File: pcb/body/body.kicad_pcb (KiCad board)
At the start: 2 copper layers, 55 x 90 mm, 146 parts, among them J1 Conn_01x05_Pin, J2 Conn_01x08_Socket, J3 Output_1_2, J4 Output_3_4, J5 Headphones, J6 Headphones, J7 Headphones, J8 Barrel_Jack_Switch, J9 Battery_Power, U1 Teensy4.1, U10 SGTL5000XNLA3, U2 TL072, U3 TL072, U4 TL072, U5 AP7313-18SAG, U6 SGTL5000XNLA3, U7 TPS54331DR, U8 SGTL5000XNLA3

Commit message: initial layout
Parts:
- removed the J6 at (124.3, 121.9)
- removed the J7 at (99.5, 121.9)
- removed the R11 at (13.6, 44.2)
- removed the R23 at (148.4, 105.0)
- removed the R25 at (148.4, 109.1)
- removed the R37 at (14.6, 12.1)
- removed the R39 at (14.6, 16.2)
- removed the R9 at (13.6, 40.1)
- added RV1: 10k, Potentiometer_THT:Potentiometer_Bourns_3296W_Vertical, F.Cu at (62.5, 110.0)
- added RV2: 10k, Potentiometer_THT:Potentiometer_Bourns_3296W_Vertical, F.Cu at (74.5, 110.0)
- added RV3: 10k, Potentiometer_THT:Potentiometer_Bourns_3296W_Vertical, F.Cu at (35.0, 126.0)
- added RV4: 10k, Potentiometer_THT:Potentiometer_Bourns_3296W_Vertical, F.Cu at (46.0, 126.0)
- added RV5: 10k, Potentiometer_THT:Potentiometer_Bourns_3296W_Vertical, F.Cu at (9.08, 126.0)
- added RV6: 10k, Potentiometer_THT:Potentiometer_Bourns_3296W_Vertical, F.Cu at (20.1, 126.0)
- J1, U1: moved to B.Cu
- J5: value Headphones -> AudioJack3_SwitchTR; footprint Connector_PinHeader_2.54mm:PinHeader_1x03_P2.54mm_Vertical -> Connector_Audio:Jack_3.5mm_CUI_SJ1-3525N_Horizontal
- moved C9 109.1 mm to (75.0, 115.0), turned to 90 degrees
- moved R16 108.0 mm to (36.8, 97.0)
- moved R17 108.0 mm to (36.8, 99.5)
- moved R18 108.0 mm to (36.8, 102.0)
- moved R19 108.0 mm to (36.8, 109.5)
- moved R20 108.0 mm to (36.8, 112.0)
- moved C12 108.0 mm to (28.8, 97.0)
- moved C13 108.0 mm to (28.8, 99.5)
- moved C14 108.0 mm to (28.8, 102.0)
- moved C15 108.0 mm to (28.8, 104.5)
- moved C16 108.0 mm to (28.8, 107.0)
- moved C17 108.0 mm to (28.8, 109.5)
- moved C18 108.0 mm to (28.8, 112.0)
- moved C19 108.0 mm to (28.8, 114.5)
- moved D3 108.0 mm to (41.2, 98.0)
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- renumbered C46 to C19, C47 to C20, C48 to C21, C49 to C22, C50 to C23, C51 to C24, C52 to C25, C53 to C26, C54 to C27, C55 to C28, C56 to C29, C57 to C30, C58 to C31, C59 to C32, C60 to C33, C19 to C34, C20 to C35, C21 to C36, C22 to C37, C23 to C38, C24 to C39, C25 to C40, C26 to C41, C27 to C42, C28 to C43, C29 to C44, C30 to C45, C31 to C46, C32 to C47, C33 to C48, C34 to C49, C35 to C50, C36 to C51, C37 to C52, C38 to C53, C39 to C54, C40 to C55, C41 to C56, C42 to C57, C43 to C58, C44 to C59, C45 to C60, C68 to C65, C65 to C66, C66 to C68, J8 to J6, J9 to J7, JP7 to JP1, R14 to R10, R15 to R11, R16 to R12, R17 to R13, R18 to R14, R19 to R15, R20 to R16, R21 to R17, R22 to R18, R27 to R19, R28 to R20, R29 to R21, R30 to R22, R31 to R23, R32 to R24, R33 to R25, R34 to R26, R35 to R27, R36 to R28, R41 to R29, R42 to R30, R49 to R31, R50 to R32, R51 to R33, R52 to R34, R53 to R35, R54 to R36, R55 to R37, R56 to R38, R57 to R39, R43 to R40, R44 to R41, R45 to R42, R13 to R9, U6 to U5, U8 to U6, U10 to U7, U7 to U8, U5 to U9
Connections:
- U5 pad 1: Net-(J5-Pin_1) -> /codec1/HEADPHONES_L
- U5 pad 2: Net-(J5-Pin_2) -> /codec1/HEADPHONES_GND
- U5 pad 4: Net-(J5-Pin_3) -> /codec1/HEADPHONES_R
- U6 pad 1: Net-(J6-Pin_1) -> /codec2/HEADPHONES_L
- U6 pad 2: Net-(J6-Pin_2) -> /codec2/HEADPHONES_GND
- U6 pad 4: Net-(J6-Pin_3) -> /codec2/HEADPHONES_R
- U7 pad 1: Net-(J7-Pin_1) -> /codec3/HEADPHONES_L
- U7 pad 2: Net-(J7-Pin_2) -> /codec3/HEADPHONES_GND
- U7 pad 4: Net-(J7-Pin_3) -> /codec3/HEADPHONES_R
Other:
- board size 55 x 90 mm -> 80 x 120 mm

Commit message: lots more layout
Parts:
- removed the C36 at (136.8, 125.8)
- removed the C41 at (140.8, 125.8)
- removed the C42 at (140.8, 128.3)
- removed the C45 at (112.0, 125.8)
- removed the C50 at (116.0, 125.8)
- removed the C51 at (116.0, 128.3)
- removed the C54 at (87.2, 125.8)
- removed the C59 at (91.2, 125.8)
- removed the C60 at (91.2, 128.3)
- removed the J3 at (90.0, 38.2)
- removed the R31 at (144.8, 120.8)
- removed the R32 at (144.8, 123.3)
- removed the R34 at (120.0, 120.8)
- removed the R35 at (120.0, 123.3)
- removed the R37 at (95.2, 120.8)
- removed the R38 at (95.2, 123.3)
- added C1: 1uF, Capacitor_SMD:C_0603_1608Metric, F.Cu at (80.2, 24.5)
- added C2: 1uF, Capacitor_SMD:C_0603_1608Metric, F.Cu at (80.2, 27.0)
- added C3: 1uF, Capacitor_SMD:C_0603_1608Metric, F.Cu at (80.2, 29.5)
- added C4: 1uF, Capacitor_SMD:C_0603_1608Metric, F.Cu at (80.2, 32.0)
- added H1: MountingHole, MountingHole:MountingHole_3.2mm_M3, F.Cu at (0.00, -10.0)
- added H2: MountingHole, MountingHole:MountingHole_3.2mm_M3, F.Cu at (70.0, -10.0)
- added H3: MountingHole, MountingHole:MountingHole_3.2mm_M3, F.Cu at (0.00, 100.0)
- added H4: MountingHole, MountingHole:MountingHole_3.2mm_M3, F.Cu at (70.0, 100.0)
- added J2: BRIDGE_GROUND, Connector_PinHeader_2.54mm:PinHeader_1x02_P2.54mm_Horizontal, F.Cu at (62.3, 93.6)
- added J7: OUTPUTS_234, Connector_PinHeader_2.54mm:PinHeader_1x06_P2.54mm_Vertical, F.Cu at (71.2, 13.0)
- added J8: 9V_POWER_INPUT, Connector_PinHeader_2.54mm:PinHeader_1x02_P2.54mm_Horizontal, F.Cu at (9.28, 93.6)
- added R1: 2.2k, Resistor_SMD:R_0603_1608Metric, F.Cu at (149.2, 91.5)
- added R10: 100R, Resistor_SMD:R_0603_1608Metric, F.Cu at (88.2, 27.0)
- added R11: 100R, Resistor_SMD:R_0603_1608Metric, F.Cu at (88.2, 29.5)
- added R12: 100R, Resistor_SMD:R_0603_1608Metric, F.Cu at (88.2, 32.0)
- added R2: 2.2k, Resistor_SMD:R_0603_1608Metric, F.Cu at (149.2, 94.0)
- added R3: 47R, Resistor_SMD:R_0603_1608Metric, F.Cu at (20.5, 94.2)
- added R4: 47R, Resistor_SMD:R_0603_1608Metric, F.Cu at (18.0, 94.2)
- added R5: 47k, Resistor_SMD:R_0603_1608Metric, F.Cu at (84.2, 24.5)
- added R6: 47k, Resistor_SMD:R_0603_1608Metric, F.Cu at (84.2, 27.0)
- added R7: 47k, Resistor_SMD:R_0603_1608Metric, F.Cu at (84.2, 29.5)
- added R8: 47k, Resistor_SMD:R_0603_1608Metric, F.Cu at (84.2, 32.0)
- added R9: 100R, Resistor_SMD:R_0603_1608Metric, F.Cu at (88.2, 24.5)
- J1: value Conn_01x05_Pin -> FRETBOARD_CONNECTION
- J4: value Output_3_4 -> MIDI_OUTPUT; footprint Connector_PinHeader_2.54mm:PinHeader_1x04_P2.54mm_Vertical -> Connector_PinHeader_2.54mm:PinHeader_1x03_P2.54mm_Horizontal
- J6: value Barrel_Jack_Switch -> MAIN_OUTPUT; footprint Connector_BarrelJack:BarrelJack_Horizontal -> Connector_PinHeader_2.54mm:PinHeader_1x02_P2.54mm_Horizontal
- RV1, RV2, RV3, RV4, RV5, RV6: footprint Potentiometer_THT:Potentiometer_Bourns_3296W_Vertical -> Potentiometer_THT:Potentiometer_Bourns_3296P_Horizontal
- moved C56 167.7 mm to (218.4, 44.3)
- moved JP1 167.7 mm to (210.0, 44.4)
- moved C63 167.7 mm to (210.3, 49.4)
- moved D7 167.7 mm to (216.9, 56.6)
- moved L1 167.7 mm to (215.3, 49.4)
- moved U8 167.7 mm to (211.4, 56.4)
- moved U9 167.7 mm to (214.7, 44.1)
- moved U7 132.9 mm to (32.4, 17.4), turned to 90 degrees
- moved U5 132.2 mm to (31.4, 72.4), turned to 90 degrees
- moved R45 131.2 mm to (31.8, 11.0), turned to 90 degrees
- moved U6 130.5 mm to (31.4, 40.6), turned to 90 degrees
- moved R43 128.7 mm to (30.8, 66.0), turned to 90 degrees
- moved R44 127.9 mm to (30.8, 34.2), turned to 90 degrees
- moved C52 124.0 mm to (26.8, 20.0), turned to -90 degrees
- moved C40 123.1 mm to (25.8, 75.0), turned to -90 degrees
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- renumbered C6 to C10, C7 to C11, C8 to C12, C9 to C13, C10 to C14, C11 to C15, C12 to C16, C13 to C17, C14 to C18, C15 to C19, C16 to C20, C17 to C21, C18 to C22, C19 to C23, C20 to C24, C21 to C25, C22 to C26, C23 to C27, C24 to C28, C25 to C29, C26 to C30, C27 to C31, C28 to C32, C29 to C33, C30 to C34, C31 to C35, C32 to C36, C33 to C37, C34 to C38, C35 to C39, C37 to C40, C38 to C41, C39 to C42, C40 to C43, C43 to C44, C44 to C45, C1 to C5, C52 to C50, C53 to C51, C55 to C52, C56 to C53, C57 to C54, C58 to C55, C61 to C56, C62 to C57, C63 to C58, C64 to C59, C2 to C6, C65 to C60, C66 to C61, C67 to C62, C68 to C63, C3 to C7, C4 to C8, C5 to C9, J2 to J3, J7 to J9, R1 to R13, R2 to R14, R3 to R15, R4 to R16, R5 to R17, R6 to R18, R7 to R19, R8 to R20, R9 to R21, R10 to R22, R11 to R23, R12 to R24, R13 to R25, R14 to R26, R15 to R27, R16 to R28, R17 to R29, R18 to R30, R19 to R31, R20 to R32, R21 to R33, R22 to R34, R23 to R35, R24 to R36, R25 to R37, R26 to R38, R27 to R39, R28 to R40, R29 to R41, R30 to R42, R33 to R43, R36 to R44, R39 to R45, R40 to R46, R41 to R47, R42 to R48
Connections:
- J4 pad 1: /codec2/LINE_OUT_L -> /MIDI_PIN_4
- J4 pad 2: GND -> /MIDI_PIN_5
- J6 pad 1: GND -> Net-(J6-Pin_1)
- J6 pad 2: +9V -> GND
- U1 pad 3: unconnected-(U1-1_TX1_CTX2_MISO1-Pad3) -> MIDI_OUT
- U5 pad 6: Net-(U5-LINEOUT_R) -> /codec1/LINE_OUT_R
- U5 pad 7: Net-(U5-LINEOUT_L) -> /codec1/LINE_OUT_L
- U6 pad 6: Net-(U6-LINEOUT_R) -> /codec2/LINE_OUT_R
- U6 pad 7: Net-(U6-LINEOUT_L) -> /codec2/LINE_OUT_L
- U7 pad 6: Net-(U7-LINEOUT_R) -> /codec3/LINE_OUT_R
- U7 pad 7: Net-(U7-LINEOUT_L) -> /codec3/LINE_OUT_L
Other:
- outline, holes or cut-outs redrawn
- board text added: "External connection cavity is roughly here (for jack out, 9V in, MIDI out, headphone out)"

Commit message: more layout...
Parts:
- J2, J4, J6, J8: moved to B.Cu
- moved C56 192.6 mm to (30.9, 88.4), turned to 180 degrees
- moved U9 190.1 mm to (30.7, 92.2), turned to 180 degrees
- moved JP1 186.5 mm to (31.0, 96.8), turned to 180 degrees
- moved L1 184.2 mm to (36.0, 91.6), turned to 180 degrees
- moved C63 180.6 mm to (36.0, 96.5), turned to 180 degrees
- moved D7 176.9 mm to (43.2, 89.9), turned to 180 degrees
- moved U8 172.9 mm to (43.0, 95.4), turned to 180 degrees
- moved R1 94.9 mm to (60.0, 59.0)
- moved R2 94.9 mm to (60.0, 61.5)
- moved R48 91.5 mm to (28.1, 101.8), turned to -90 degrees
- moved R47 86.5 mm to (30.6, 101.8), turned to -90 degrees
- moved R46 81.5 mm to (33.1, 101.8), turned to -90 degrees
- moved C60 76.5 mm to (35.6, 101.8), turned to -90 degrees
- moved C62 71.6 mm to (38.1, 101.8), turned to -90 degrees
- moved C61 66.6 mm to (40.6, 101.8), turned to -90 degrees
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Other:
- board text added: "GK3 cable"

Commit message: haven't committed for a bit
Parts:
- removed the J4 at (7.00, 74.5)
- removed the J6 at (7.00, 83.7)
- removed J8: 9V_POWER_INPUT, Connector_PinHeader_2.54mm:PinHeader_1x02_P2.54mm_Horizontal
- added J5: External_connections, Connector_PinHeader_2.54mm:PinHeader_1x07_P2.54mm_Horizontal, B.Cu at (6.00, 74.8)
- moved J6 47.1 mm to (29.0, -8.08), turned to 0 degrees
- moved J7 45.7 mm to (55.5, 101.3), turned to 180 degrees
- moved C1 45.0 mm to (80.2, 69.5)
- moved C2 45.0 mm to (80.2, 72.0)
- moved C3 45.0 mm to (80.2, 74.5)
- moved C4 45.0 mm to (80.2, 77.0)
- moved R10 45.0 mm to (88.2, 72.0)
- moved R11 45.0 mm to (88.2, 74.5)
- moved R12 45.0 mm to (88.2, 77.0)
- moved R3 45.0 mm to (84.2, 69.5)
- moved R4 45.0 mm to (84.2, 72.0)
- moved R6 45.0 mm to (84.2, 74.5)
- moved R7 45.0 mm to (84.2, 77.0)
- moved R9 45.0 mm to (88.2, 69.5)
- moved R5 20.8 mm to (10.0, 75.0), turned to 0 degrees
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- renumbered J5 to J4, J7 to J6, J9 to J7, R5 to R3, R6 to R4, R4 to R5, R7 to R6, R8 to R7, R3 to R8
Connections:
- R9 pad 1: Net-(J6-Pin_1) (its old number) -> MAIN_OUTPUT
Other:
- board size 80 x 120 mm -> 90 x 120 mm
- board text added: "leave some space for analog connections"

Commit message: first four layer board...
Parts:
- moved J6 111.0 mm to (8.38, 101.0), turned to 90 degrees
- moved R10 83.5 mm to (8.50, 97.0), turned to 90 degrees
- moved R9 79.4 mm to (10.0, 83.5)
- moved R11 78.0 mm to (13.5, 97.0), turned to 90 degrees
- moved R12 72.5 mm to (18.5, 97.0), turned to 90 degrees
- moved R7 58.0 mm to (39.5, 40.0), turned to 180 degrees
- moved C4 56.3 mm to (36.0, 42.0)
- moved C3 56.0 mm to (36.0, 40.0)
- moved R4 53.8 mm to (39.5, 42.0), turned to 180 degrees
- moved R3 44.9 mm to (39.5, 74.0), turned to 180 degrees
- moved R6 44.7 mm to (39.5, 72.0), turned to 180 degrees
- moved C1 44.2 mm to (36.0, 72.0)
- moved C2 44.2 mm to (36.0, 74.0)
- moved J3 12.1 mm to (25.0, 47.5)
- moved C13 4.51 mm to (9.00, 71.5)
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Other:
- copper layers 2 -> 4

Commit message: 4 layer routing...
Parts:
- moved R1 113.1 mm to (165.0, 101.0), turned to 180 degrees
- moved C44 112.4 mm to (138.8, 73.2)
- moved C45 112.4 mm to (138.8, 75.2)
- moved J1 112.4 mm to (153.1, 46.0)
- moved J7 112.4 mm to (160.5, 141.3)
- moved R44 112.4 mm to (135.8, 74.2)
- moved C1 112.4 mm to (141.0, 112.0)
- moved C10 112.4 mm to (120.2, 109.5)
- moved C11 112.4 mm to (125.2, 102.5)
- moved C12 112.4 mm to (114.0, 93.5)
- moved C13 112.4 mm to (114.0, 111.5)
- moved C16 112.4 mm to (125.2, 65.0)
- moved C17 112.4 mm to (125.2, 79.0)
- moved C18 112.4 mm to (125.2, 69.0)
- moved C19 112.4 mm to (125.2, 75.0)
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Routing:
- net Net-(C9-Pad2): track 0.00 -> 31.8 mm
- net Net-(C31-Pad2): track 0.00 -> 31.8 mm
- net Net-(C20-Pad2): track 0.00 -> 31.8 mm
- net Net-(C21-Pad2): track 0.00 -> 28.5 mm, vias 0 -> 2
- net Net-(C32-Pad2): track 0.00 -> 28.5 mm, vias 0 -> 2
- net Net-(C10-Pad2): track 0.00 -> 28.5 mm, vias 0 -> 2
- net Net-(U4B--): track 0.00 -> 27.0 mm
- net Net-(U2B--): track 0.00 -> 27.0 mm
- net Net-(U3B--): track 0.00 -> 27.0 mm
- net Net-(U3A--): track 0.00 -> 24.8 mm
- net Net-(U2A--): track 0.00 -> 24.8 mm
- net Net-(U4A--): track 0.00 -> 24.8 mm
- net +3.3V: track 0.00 -> 21.3 mm
- net /codec3/LINE_IN_R: track 0.00 -> 20.5 mm
- net /codec2/LINE_IN_R: track 0.00 -> 20.5 mm
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- added copper zone on In1.Cu, net GND
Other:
- board text removed: "leave some space for analog connections"

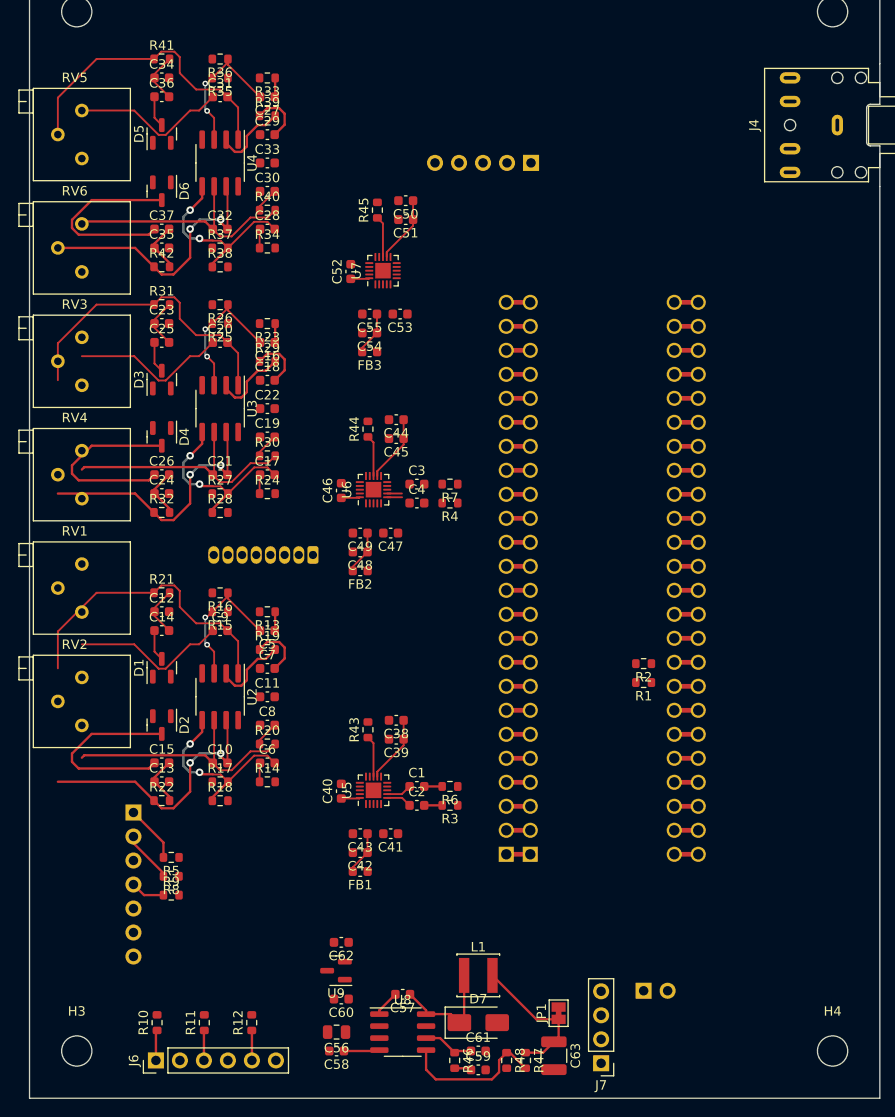
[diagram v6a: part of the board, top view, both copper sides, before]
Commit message: routing going well with 4 layers
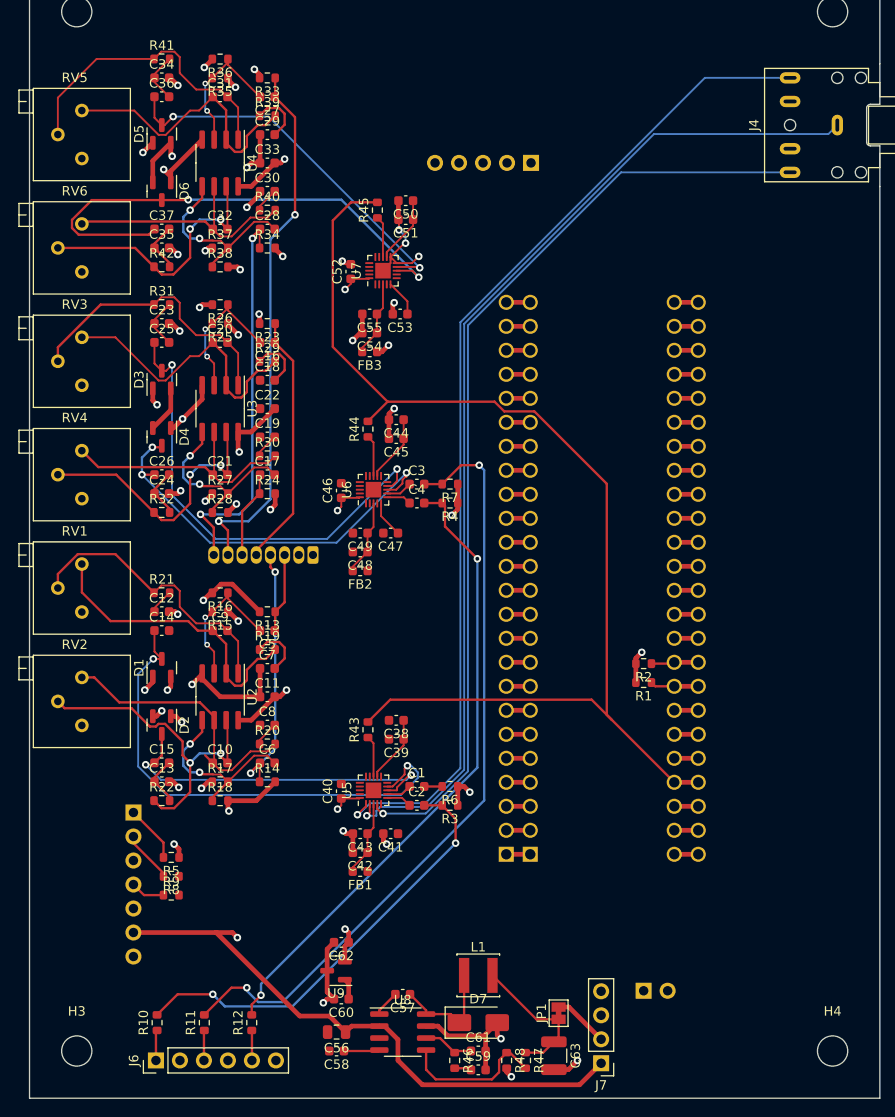
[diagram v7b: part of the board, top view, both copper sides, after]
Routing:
- net GND: track 0.00 -> 131.3 mm, vias 0 -> 40
- net DAC_MCLK: track 2.54 -> 121.6 mm
- net /codec1/HEADPHONES_GND: track 0.00 -> 109.4 mm, vias 0 -> 1
- net /codec1/HEADPHONES_L: track 0.00 -> 107.3 mm, vias 0 -> 1
- net /codec1/HEADPHONES_R: track 0.00 -> 100.2 mm, vias 0 -> 1
- net +9V: track 0.00 -> 88.9 mm, vias 0 -> 10
- net Net-(C3-Pad2): track 0.00 -> 82.8 mm, vias 0 -> 2
- net Net-(C4-Pad2): track 0.00 -> 67.5 mm, vias 0 -> 2
- net /pickuppair3/INPUT_1: track 2.02 -> 57.0 mm, vias 0 -> 2
- net /codec1/LINE_IN_L: track 3.32 -> 53.3 mm, vias 0 -> 2
- net /codec2/LINE_IN_L: track 3.32 -> 49.8 mm, vias 0 -> 2
- net Net-(C2-Pad2): track 1.90 -> 46.7 mm, vias 0 -> 2
- net /pickuppair3/INPUT_2: track 2.02 -> 42.1 mm, vias 0 -> 2
- net /codec3/LINE_IN_L: track 3.32 -> 40.1 mm, vias 0 -> 2
- net /codec3/LINE_IN_R: track 20.5 -> 53.7 mm, vias 0 -> 2
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- added copper zone on In2.Cu, net +1V8
- added copper zone on In2.Cu, net +3.3V
- added copper zone on In2.Cu, net +9V

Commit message: zero unrouted for now
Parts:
- moved C52 1.04 mm to (133.0, 57.8)
- moved C40 1.00 mm to (132.0, 112.5)
- moved C46 1.00 mm to (132.0, 80.7)
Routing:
- net DAC_LRCLK: track 2.54 -> 147.0 mm, vias 0 -> 7
- net DAC_BCLK: track 2.54 -> 146.1 mm, vias 0 -> 9
- net DAC_SCL: track 5.12 -> 126.6 mm, vias 0 -> 7
- net DAC_SDA: track 5.01 -> 104.3 mm, vias 0 -> 3
- net CODEC3_DIN: track 2.54 -> 69.3 mm, vias 0 -> 1
- net MIDI_OUT: track 2.54 -> 46.1 mm
- net CODEC2_DIN: track 2.54 -> 43.1 mm, vias 0 -> 2
- net Net-(C1-Pad2): track 1.90 -> 39.8 mm, vias 0 -> 2
- net GND: track 131.3 -> 163.5 mm, vias 40 -> 52
- net CODEC2_DOUT: track 2.54 -> 30.8 mm, vias 0 -> 2
- net CODEC1_DIN: track 2.54 -> 30.6 mm
- net CODEC1_DOUT: track 2.54 -> 28.1 mm
- net +3.3V: track 44.3 -> 61.0 mm, vias 6 -> 15
- net Net-(C12-Pad1): track 2.66 -> 8.94 mm, vias 0 -> 2
- net Net-(U5-VAG): track 0.00 -> 3.99 mm
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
